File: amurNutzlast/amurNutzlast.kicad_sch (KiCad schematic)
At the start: 0 parts

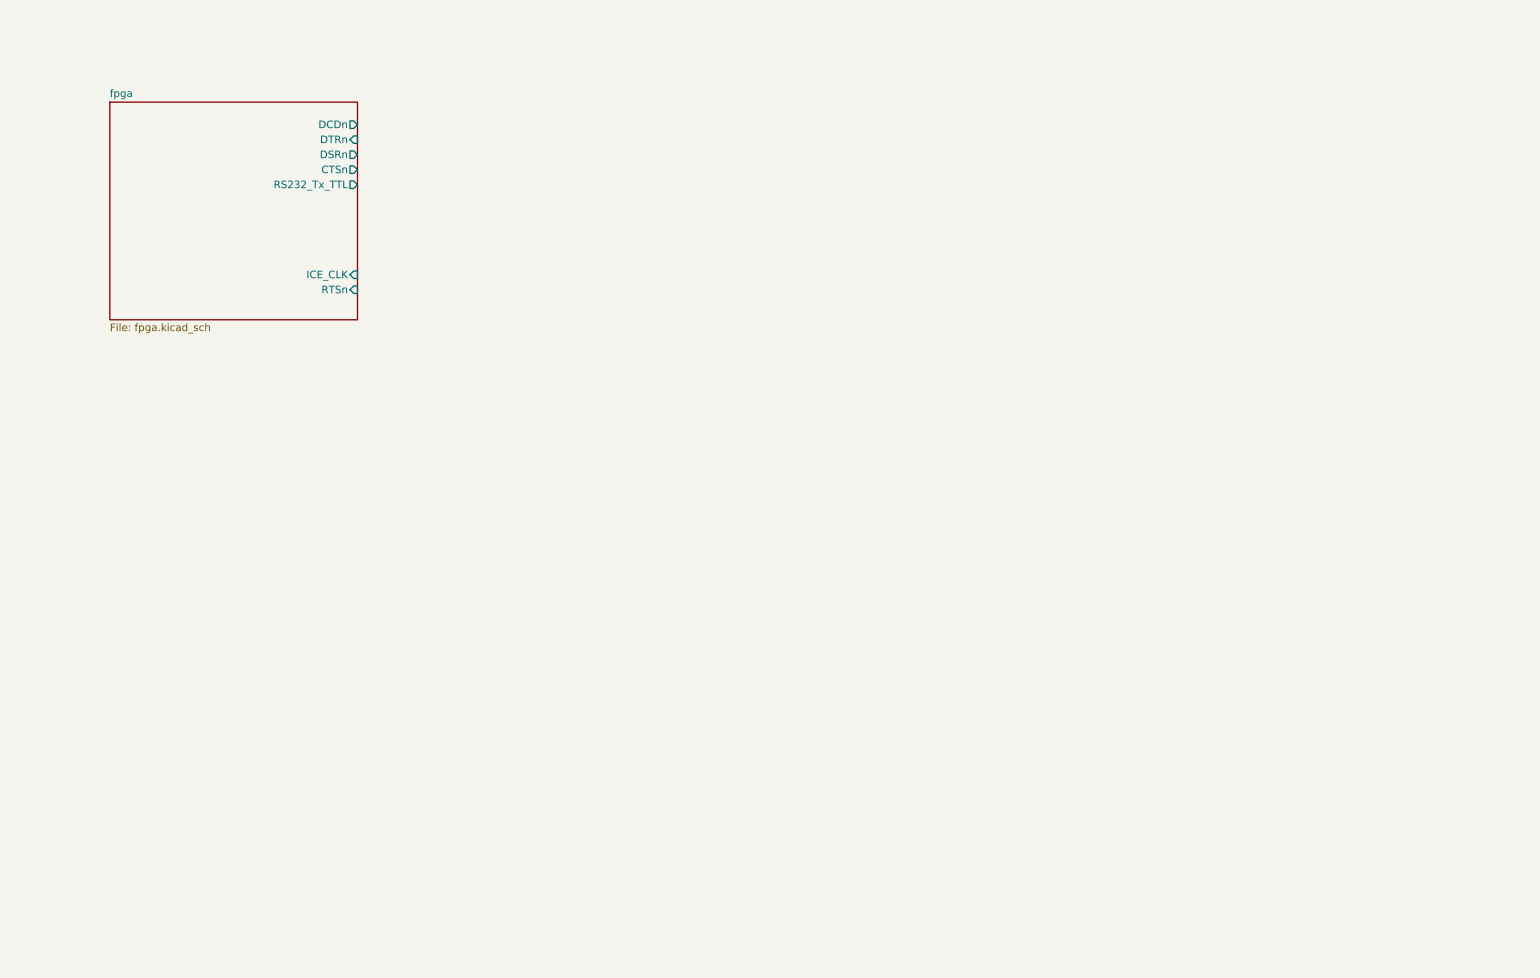
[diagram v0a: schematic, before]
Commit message: working on the FTDI design in kicad FPGA prototype board
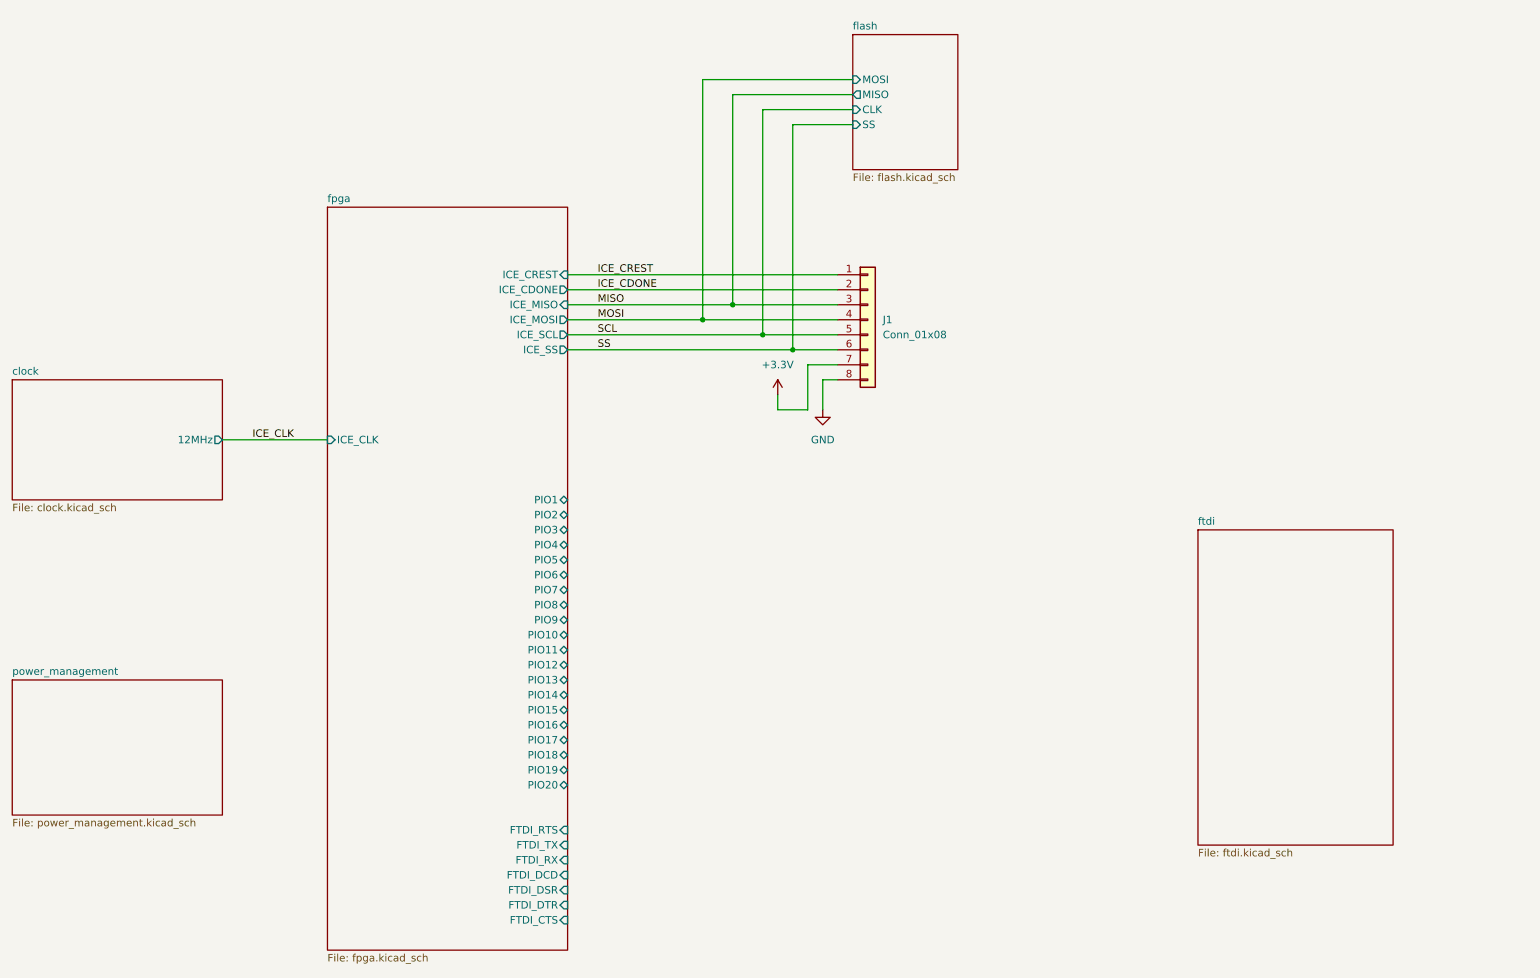
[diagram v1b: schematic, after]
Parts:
- added J1: Conn_01x08, Connector_PinHeader_2.54mm:PinHeader_2x04_P2.54mm_Vertical, symbol Connector_Generic:Conn_01x08
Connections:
- new net +3.3V: J1.7 (Pin_7)
- new net GND: J1.8 (Pin_8)
- new net ICE_CDONE: J1.2 (Pin_2)
- new net ICE_CREST: J1.1 (Pin_1)
- new net MISO: J1.3 (Pin_3)
- new net MOSI: J1.4 (Pin_4)
- new net SCL: J1.5 (Pin_5)
- new net SS: J1.6 (Pin_6)
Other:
- added sheet clock (clock.kicad_sch)
- added sheet flash (flash.kicad_sch)
- added sheet ftdi (ftdi.kicad_sch)
- added sheet power_management (power_management.kicad_sch)
- sheet fpga ports: added FTDI_CTS, FTDI_DCD, FTDI_DSR, FTDI_DTR, FTDI_RTS, FTDI_RX, FTDI_TX, ICE_CDONE, ICE_CREST, ICE_MISO, ICE_MOSI, ICE_SCL, ICE_SS, PIO1, PIO10, PIO11, PIO12, PIO13, PIO14, PIO15, PIO16, PIO17, PIO18, PIO19, PIO2, PIO20, PIO3, PIO4, PIO5, PIO6, PIO7, PIO8, PIO9; removed CTSn, DCDn, DSRn, DTRn, RS232_Tx_TTL, RTSn

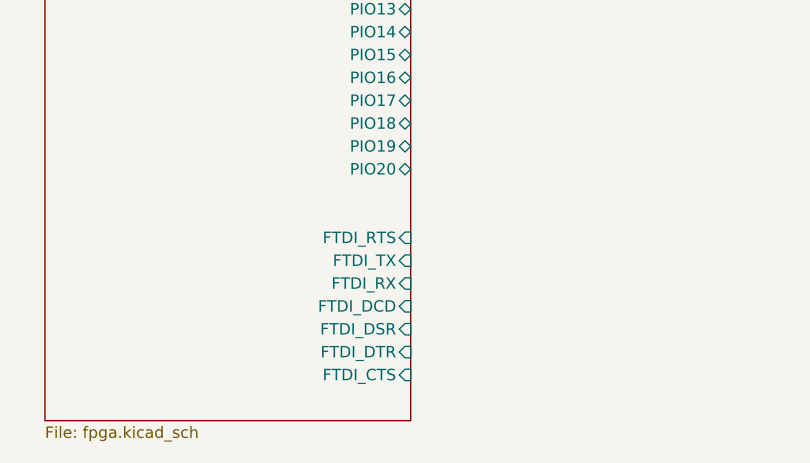
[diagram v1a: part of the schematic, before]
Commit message: ftdi schematic was added apart of the USB
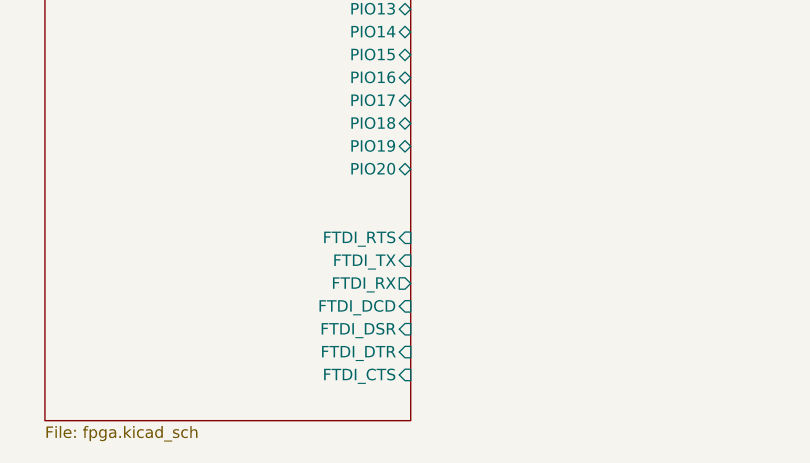
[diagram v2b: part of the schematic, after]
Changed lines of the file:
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@@
-      (effects (font (size 1.27 1.27)) (justify right))
-    )
-    (pin "FTDI_RX" input (at 111.76 157.48 0)
       (effects (font (size 1.27 1.27)) (justify right))
     )
@@
       (effects (font (size 1.27 1.27)) (justify right))
     )
+    (pin "FTDI_RX" output (at 111.76 157.48 0)
+      (effects (font (size 1.27 1.27)) (justify right))
+    )

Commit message: finisched design schematics + pdf
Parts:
- added J3: Conn_01x02, symbol Connector_Generic:Conn_01x02
- added J5, J7: Conn_01x07, symbol Connector_Generic:Conn_01x07
- added J6: Conn_01x06, symbol Connector_Generic:Conn_01x06
- added J8: Conn_01x20, symbol Connector_Generic:Conn_01x20
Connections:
- net GND: now also J3.1 (Pin_1)
- net fpga/FTDI_CTS: now also J7.7 (Pin_7)
- net fpga/FTDI_DCD: now also J7.4 (Pin_4)
- net fpga/FTDI_DSR: now also J7.5 (Pin_5)
- net fpga/FTDI_DTR: now also J7.6 (Pin_6)
- net fpga/FTDI_RTS: now also J7.1 (Pin_1)
- net fpga/FTDI_RX: now also J7.3 (Pin_3)
- net fpga/FTDI_TX: now also J7.2 (Pin_2)
- net fpga/PIO1: now also J8.1 (Pin_1)
- net fpga/PIO10: now also J8.10 (Pin_10)
- net fpga/PIO11: now also J8.11 (Pin_11)
- net fpga/PIO12: now also J8.12 (Pin_12)
- net fpga/PIO13: now also J8.13 (Pin_13)
- net fpga/PIO14: now also J8.14 (Pin_14)
- net fpga/PIO15: now also J8.15 (Pin_15)
- net fpga/PIO16: now also J8.16 (Pin_16)
- net fpga/PIO17: now also J8.17 (Pin_17)
- net fpga/PIO18: now also J8.18 (Pin_18)
- net fpga/PIO19: now also J8.19 (Pin_19)
- net fpga/PIO2: now also J8.2 (Pin_2)
- net fpga/PIO20: now also J8.20 (Pin_20)
- net fpga/PIO3: now also J8.3 (Pin_3)
- net fpga/PIO4: now also J8.4 (Pin_4)
- net fpga/PIO5: now also J8.5 (Pin_5)
- net fpga/PIO6: now also J8.6 (Pin_6)
- net fpga/PIO7: now also J8.7 (Pin_7)
- net fpga/PIO8: now also J8.8 (Pin_8)
- net fpga/PIO9: now also J8.9 (Pin_9)
- new net +5V: J3.2 (Pin_2)
- new net ftdi/CTS: J5.1 (Pin_1)
- new net ftdi/DCD: J5.4 (Pin_4)
- new net ftdi/DSR: J5.3 (Pin_3)
- new net ftdi/DTR: J5.2 (Pin_2)
- new net ftdi/ICE_CDONE: J6.5 (Pin_5)
- new net ftdi/ICE_CLK: J6.2 (Pin_2)
- new net ftdi/ICE_CREST: J6.6 (Pin_6)
- new net ftdi/ICE_MISO: J6.4 (Pin_4)
- new net ftdi/ICE_MOSI: J6.3 (Pin_3)
- new net ftdi/ICE_SS: J6.1 (Pin_1)
- new net ftdi/RTS: J5.7 (Pin_7)
- new net ftdi/RX: J5.5 (Pin_5)
- new net ftdi/TX: J5.6 (Pin_6)
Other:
- sheet ftdi ports: added CTS, DCD, DSR, DTR, ICE_CDONE, ICE_CLK, ICE_CREST, ICE_MISO, ICE_MOSI, ICE_SS, RTS, RX, TX; removed none

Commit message: layout start
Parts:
- J3: footprint (none) -> LED_SMD:LED_0603_1608Metric
- J5, J7: footprint (none) -> Connector_PinHeader_2.54mm:PinHeader_1x07_P2.54mm_Vertical
- J6: footprint (none) -> Connector_PinHeader_2.54mm:PinHeader_2x03_P2.54mm_Vertical
- J8: footprint (none) -> Connector_PinHeader_2.54mm:PinHeader_2x10_P2.54mm_Vertical
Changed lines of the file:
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@@
       (effects (font (size 1.27 1.27)))
     )
-    (property "Footprint" "" (at 177.8 116.84 0)
+    (property "Footprint" "Connector_PinHeader_2.54mm:PinHeader_2x03_P2.54mm_Vertical" (at 177.8 116.84 0)
       (effects (font (size 1.27 1.27)) hide)
     )
@@
       (effects (font (size 1.27 1.27)))
     )
-    (property "Footprint" "" (at 180.34 144.78 0)
+    (property "Footprint" "Connector_PinHeader_2.54mm:PinHeader_1x07_P2.54mm_Vertical" (at 180.34 144.78 0)
       (effects (font (size 1.27 1.27)) hide)
     )
@@
       (effects (font (size 1.27 1.27)) (justify left))
     )
-    (property "Footprint" "" (at 160.02 144.78 0)
+    (property "Footprint" "Connector_PinHeader_2.54mm:PinHeader_1x07_P2.54mm_Vertical" (at 160.02 144.78 0)
       (effects (font (size 1.27 1.27)) hide)
     )
@@
       (effects (font (size 1.27 1.27)) (justify left))
     )
-    (property "Footprint" "" (at 119.38 119.38 0)
+    (property "Footprint" "Connector_PinHeader_2.54mm:PinHeader_2x10_P2.54mm_Vertical" (at 119.38 119.38 0)
       (effects (font (size 1.27 1.27)) hide)
     )
@@
       (effects (font (size 1.27 1.27)))
     )
-    (property "Footprint" "" (at 50.8 27.94 0)
-      (effects (font (size 1.27 1.27)) hide)
-    )
+    (property "Footprint" "LED_SMD:LED_0603_1608Metric" (at 50.8 27.94 0)
+      (effects (font (size 1.27 1.27)) hide)
+    )

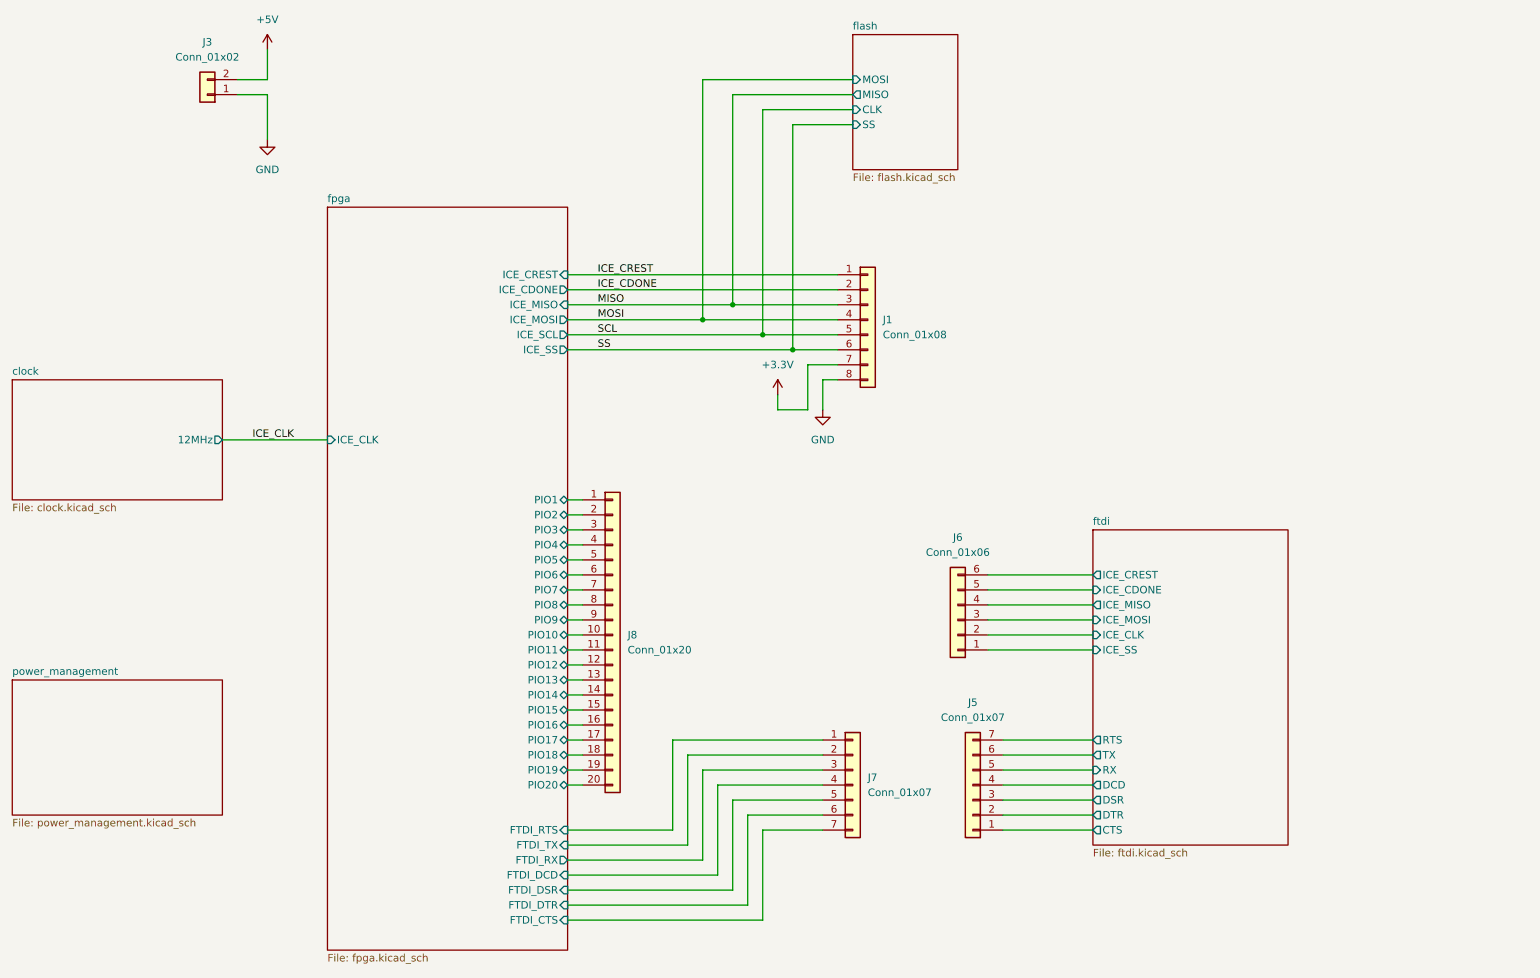
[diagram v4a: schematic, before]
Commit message: deleted 3.3 converter for ftdi and moved USB to a hierarhical sheet
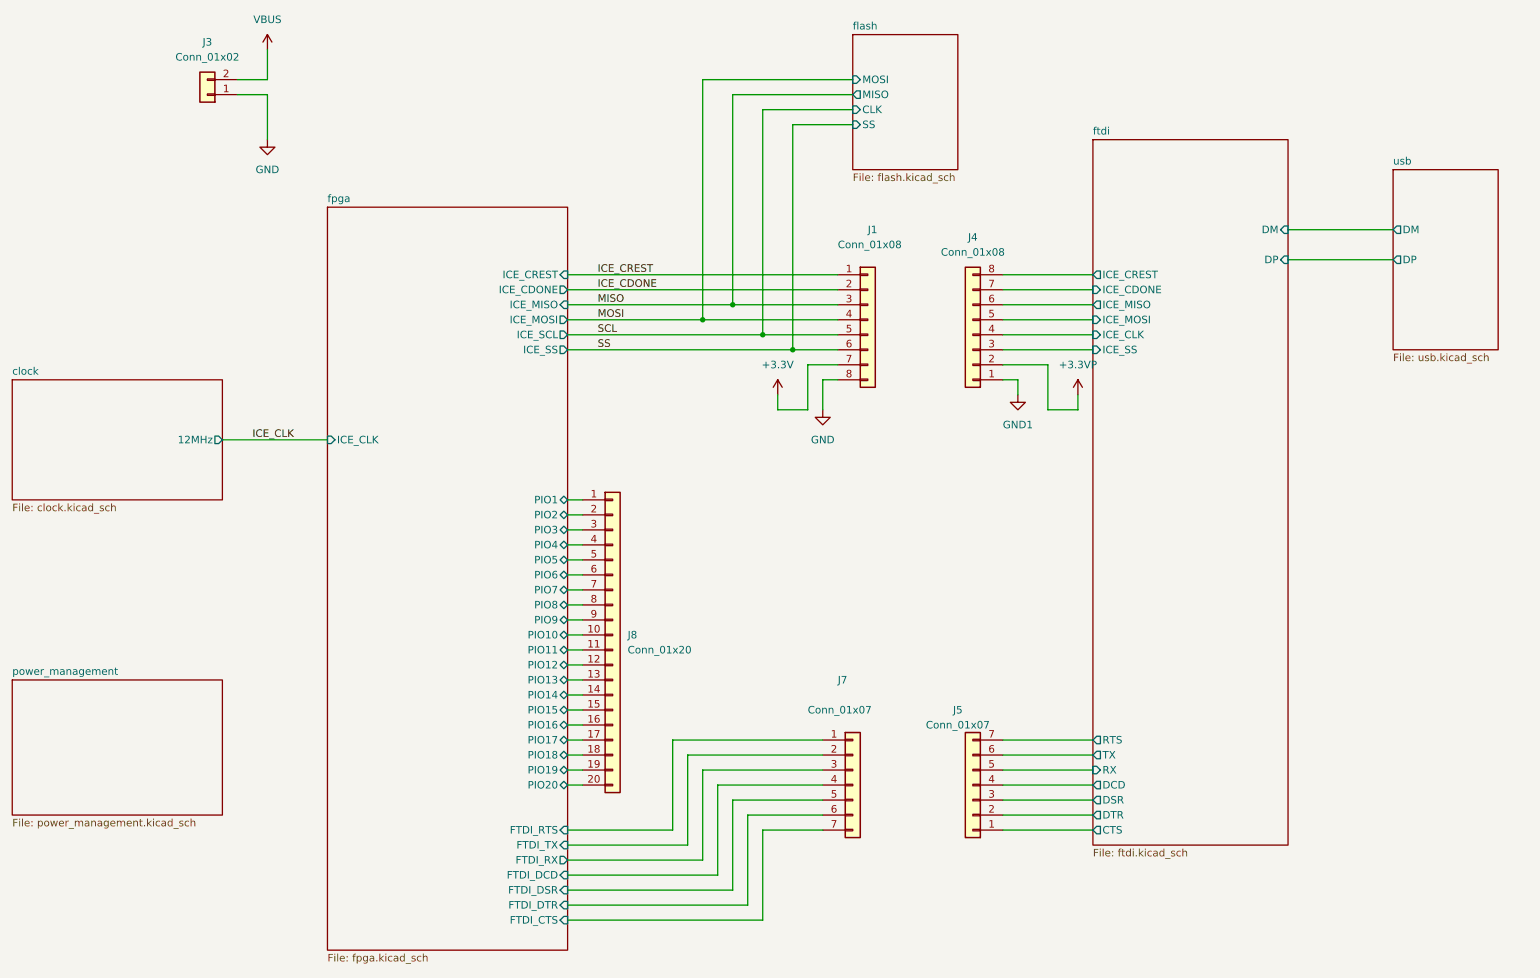
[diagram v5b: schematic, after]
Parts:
- removed J6: Conn_01x06, Connector_PinHeader_2.54mm:PinHeader_2x03_P2.54mm_Vertical, symbol Connector_Generic:Conn_01x06
- added J4: Conn_01x08, Connector_PinHeader_2.54mm:PinHeader_2x04_P2.54mm_Vertical, symbol Connector_Generic:Conn_01x08
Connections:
- net ftdi/ICE_CDONE: now also J4.7 (Pin_7)
- net ftdi/ICE_CLK: now also J4.4 (Pin_4)
- net ftdi/ICE_CREST: now also J4.8 (Pin_8)
- net ftdi/ICE_MISO: now also J4.6 (Pin_6)
- net ftdi/ICE_MOSI: now also J4.5 (Pin_5)
- net ftdi/ICE_SS: now also J4.3 (Pin_3)
- net +5V renamed VBUS
- new net +3.3VP: J4.2 (Pin_2)
- new net GND1: J4.1 (Pin_1)
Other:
- added sheet usb (usb.kicad_sch)
- sheet ftdi ports: added DM, DP; removed none
